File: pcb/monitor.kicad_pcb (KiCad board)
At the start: 2 copper layers, 111 parts, among them K1 DG128-02P, K101 DG128-02P, K102 DG128-02P, K103 DG128-02P, K104 DG128-02P, K105 DG128-02P, K106 DG128-02P, K107 DG128-02P, K108 DG128-02P, K109 DG128-02P, K110 DG128-02P, K111 DG128-02P, K112 DG128-02P, K113 JUMPER_3, K114 JUMPER_3, K2 DG128-02P, K3 DG128-02P, K4 DG128-02P, K5 DG128-02P, K6 DG128-02P, T1 ZUMT718, T10 ZUMT718, T101 ZUMT718, T102 ZUMT718, T2 ZUMT718, T3 ZUMT718, T4 ZUMT718, T5 ZUMT718, T6 ZUMT718, T7 ZUMT718, T8 ZUMT718, T9 ZUMT718, U1 LTC6803-3

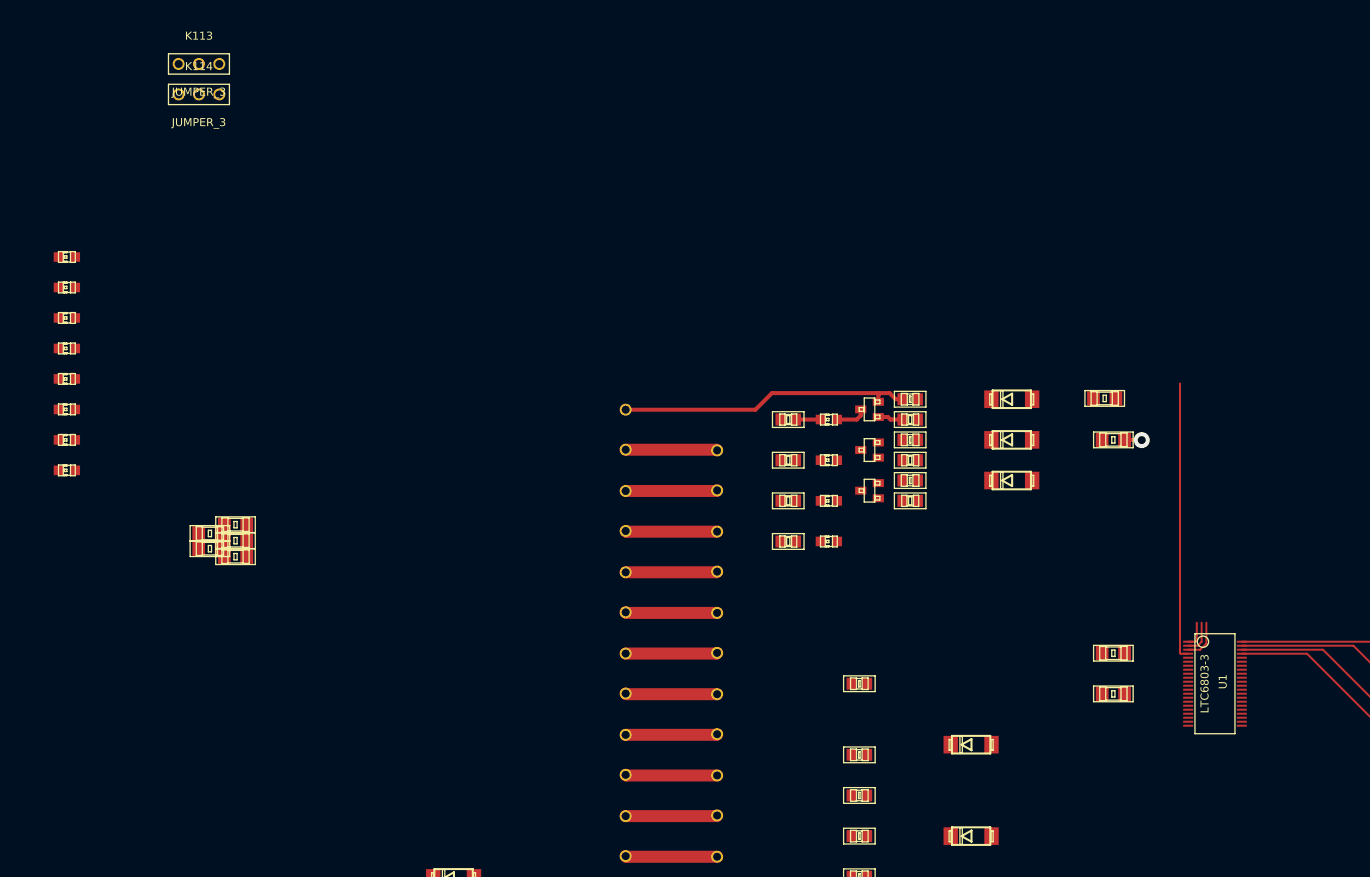
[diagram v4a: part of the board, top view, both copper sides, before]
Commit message: Change to 4 layer design
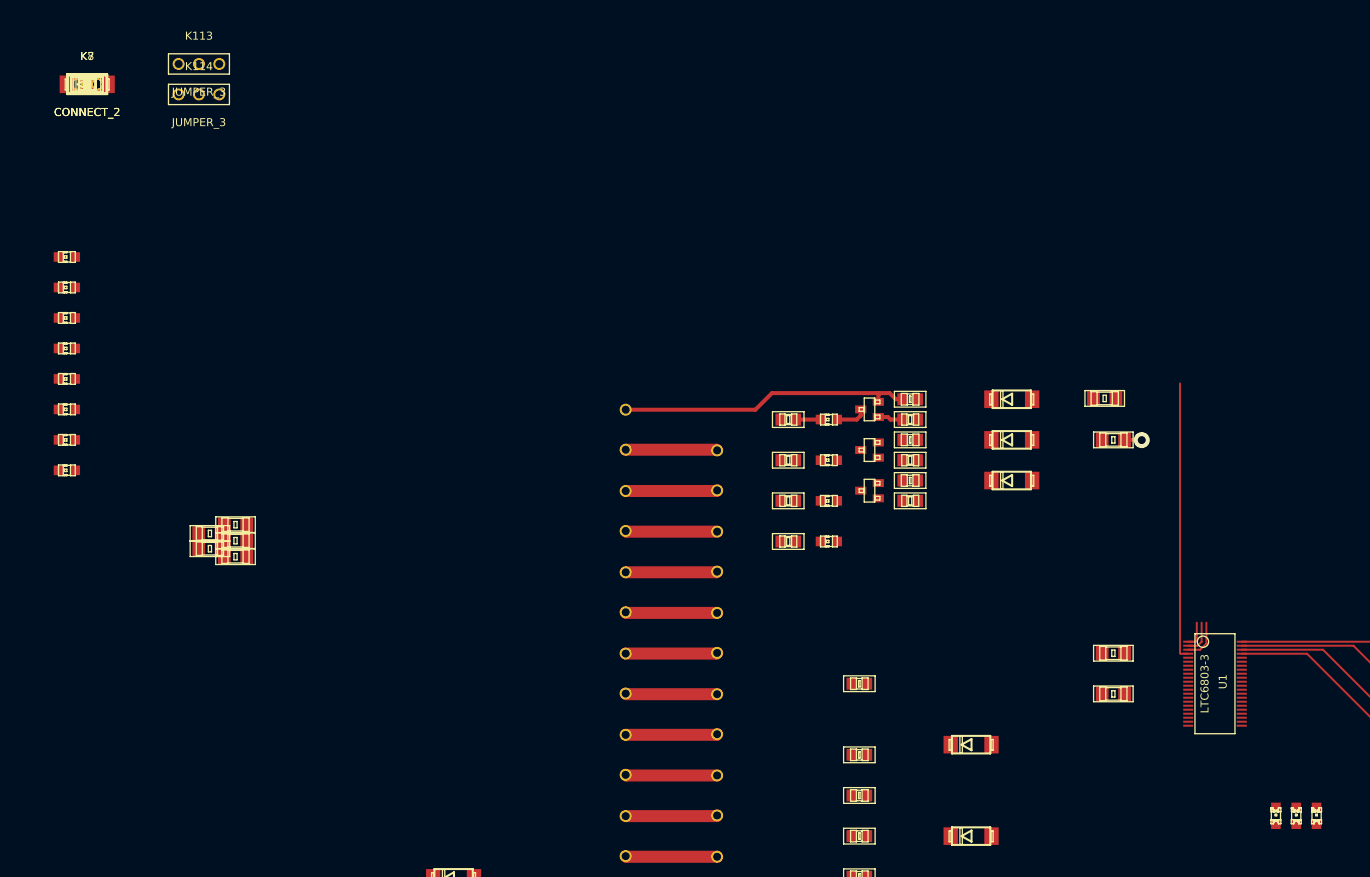
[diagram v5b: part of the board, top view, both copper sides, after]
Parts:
- added C1: 100n, oshec_rcl:rcl-C0805, F.Cu at (0.00, 0.00)
- added D4: CMHZ5265B, oshec_diode:diode-1-DO214AA, F.Cu at (0.00, 0.00)
- added K7, K8: CONNECT_2, Aalto_connect:CONNECT_2_2mm54_VERT, F.Cu at (0.00, 0.00)
- added L1: BLM31PG330SN1L, oshec_rcl:rcl-L1206, F.Cu at (0.00, 0.00)
- added LD13: LEDCHIPLED_0805, led-CHIPLED_0805, F.Cu at (153.7, 91.4)
- added LD14: LEDCHIPLED_0805, led-CHIPLED_0805, F.Cu at (151.1, 91.4)
- added LD15: LEDCHIPLED_0805, led-CHIPLED_0805, F.Cu at (148.6, 91.4)
- added R25, R26, R27: 220, oshec_rcl:rcl-R0805, F.Cu at (0.00, 0.00)
- added R28, R29: 200k, oshec_rcl:rcl-R0805, F.Cu at (0.00, 0.00)
- added R30, R31: 100, oshec_rcl:rcl-R0805, F.Cu at (0.00, 0.00)
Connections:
- K6 pad 2: /BATT1- -> GND
- R24 pad 2: /BATT1- -> GND
- T5 pad E: /BATT12+ -> /BATT6+
- U1 pad 30: GND -> /V-
- U1 pad 32: Net-(U1-Pad32) -> /Vtemp1
- U1 pad 33: Net-(U1-Pad33) -> /Vtemp2
- U1 pad 34: Net-(U1-Pad34) -> /Vref
- U1 pad 37: Net-(U1-Pad37) -> /WDTB
- U1 pad 38: Net-(U1-Pad38) -> /GPIO1
- U1 pad 39: Net-(U1-Pad39) -> /GPIO2
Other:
- copper layers 2 -> 4

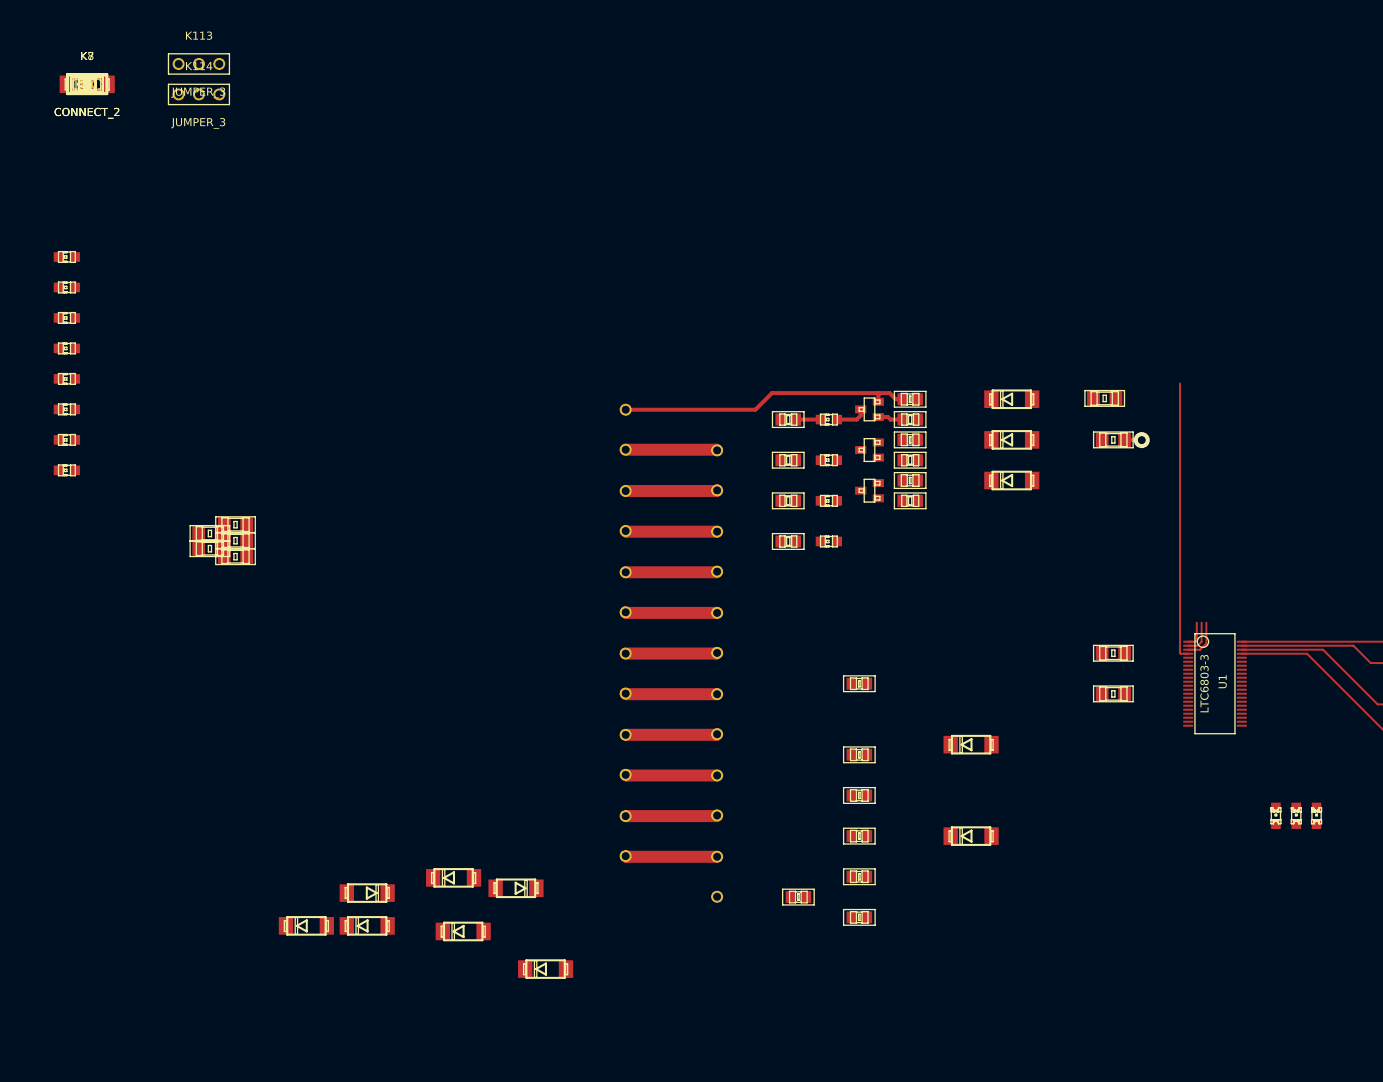
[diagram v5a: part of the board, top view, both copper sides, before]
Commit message: Add temperature + led connections
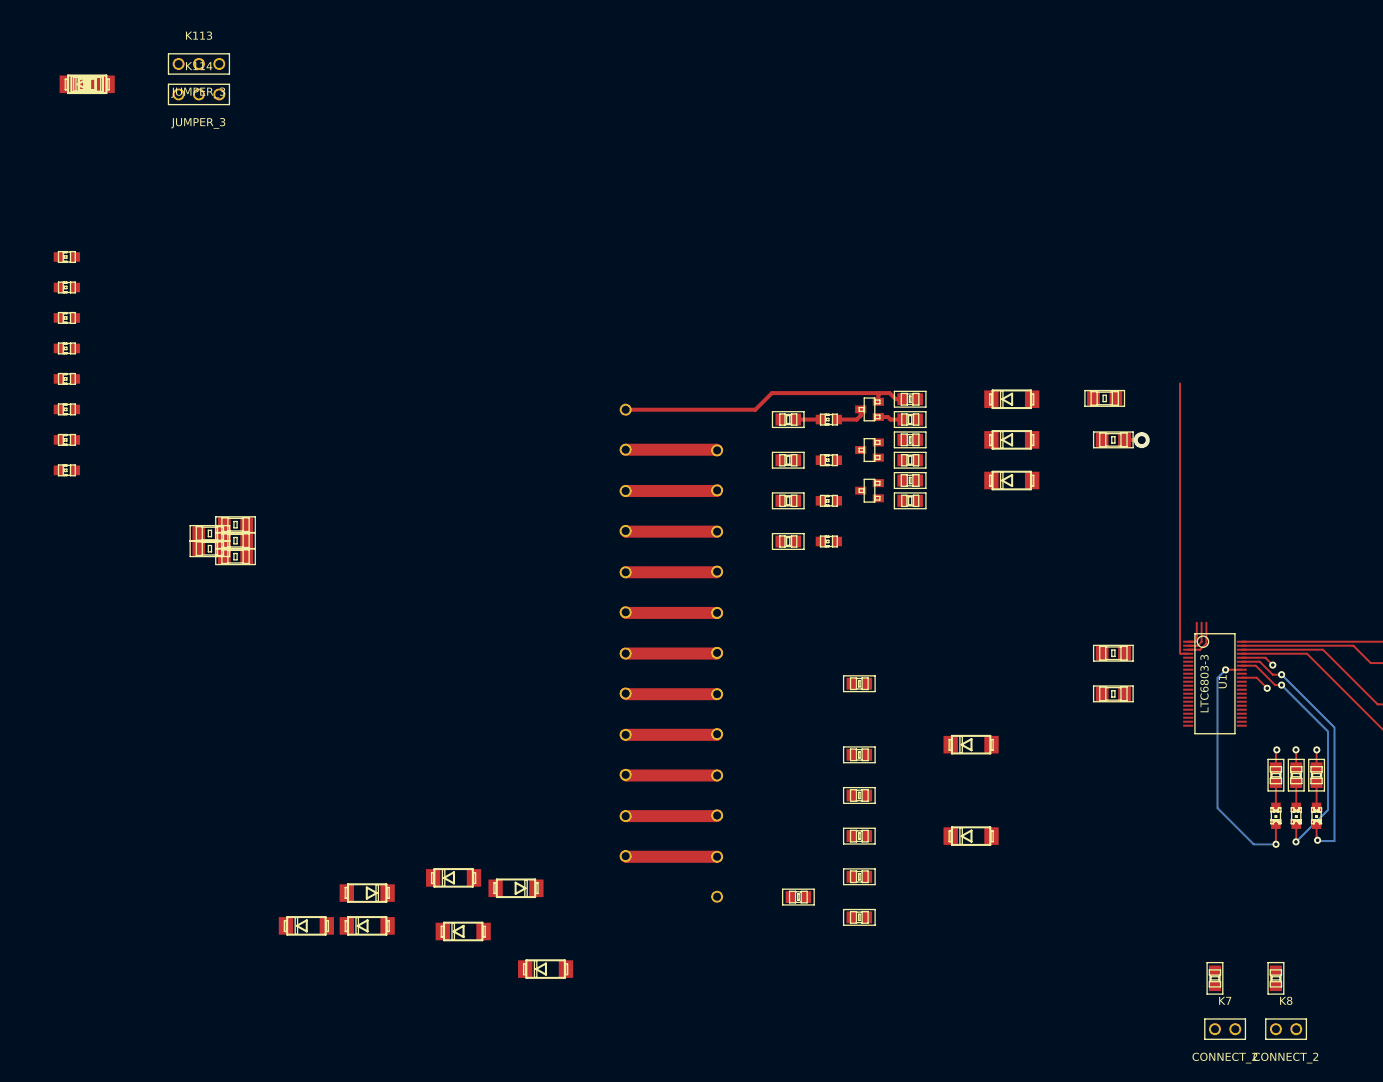
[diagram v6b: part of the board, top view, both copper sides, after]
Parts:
- moved K8 190.8 mm to (149.9, 118.1)
- moved R29 185.9 mm to (148.6, 111.8), turned to 90 degrees
- moved K7 184.9 mm to (142.2, 118.1)
- moved R28 179.9 mm to (141.0, 111.8), turned to 90 degrees
- moved R25 176.3 mm to (153.7, 86.4), turned to 270 degrees
- moved R26 174.1 mm to (151.1, 86.4), turned to 270 degrees
- moved R27 171.9 mm to (148.6, 86.4), turned to 270 degrees
- turned LD13 to 180 degrees
- turned LD14 to 180 degrees
- turned LD15 to 180 degrees
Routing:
- net /GPIO2: track 0.00 -> 33.4 mm, vias 0 -> 2
- net /GPIO1: track 0.00 -> 31.9 mm, vias 0 -> 2
- net /WDTB: track 0.00 -> 31.4 mm, vias 0 -> 2
- net /5V: track 0.00 -> 10.4 mm, vias 0 -> 4
- net /VMODE: track 0.00 -> 4.36 mm, vias 0 -> 1
- net Net-(LD15-PadA): track 0.00 -> 3.08 mm
- net Net-(LD14-PadA): track 0.00 -> 3.08 mm
- net Net-(LD13-PadA): track 0.00 -> 3.08 mm
- added copper zone on Inner1.Cu, net /5V

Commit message: Place grounds to PCB
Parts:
- removed C101, C102, C103, C104, C105, C106, C107, C108, C109, C110, C111, C112, C113: 3u3, oshec_rcl:rcl-C1206
- removed D101, D102, D103, D104, D105, D106, D107, D108, D109, D110, D111, D112: 7V5, oshec_diode:diode-1-DO214AA
- removed K1, K2: DG128-02P, Aalto_connect:CONNECT_2_5.00mm_SCREW_DG128-02P_DG128-5.0-02P-14-00A(H)
- removed LD1, LD10, LD11, LD12, LD2, LD3, LD4, LD5, LD6, LD7, LD8, LD9: GREEN-LED0805, oshec_led:led-CHIP-LED0805
- removed R1, R13, R14, R15, R16, R17, R18, R2, R3, R4, R5, R6: 10k, oshec_rcl:rcl-R0805
- removed R10, R11, R12, R19, R20, R21, R22, R23, R24, R7, R8, R9: 100, oshec_rcl:rcl-R0805
- removed R101, R102, R103, R104, R105, R106, R107, R108, R109, R110, R111, R112, R113: 10k, oshec_rcl:rcl-C0805
- removed R114: R-EU_R0805, oshec_rcl:rcl-C0805
- removed T1, T10, T101, T102, T2, T3, T4, T5, T6, T7, T8, T9: ZUMT718, oshec_transistor:transistor-SOT23-BEC
- added C301: 3u3, oshec_rcl:rcl-C1210, F.Cu at (111.8, 34.3)
- added C302: 3u3, oshec_rcl:rcl-C1210, F.Cu at (111.8, 44.5)
- added C303: 3u3, oshec_rcl:rcl-C1210, F.Cu at (111.8, 54.6)
- added C304, C305, C306, C310, C311: 3u3, oshec_rcl:rcl-C1210, F.Cu at (0.00, 0.00)
- added C307: 3u3, oshec_rcl:rcl-C1210, F.Cu at (111.8, 95.2)
- added C308: 3u3, oshec_rcl:rcl-C1210, F.Cu at (111.8, 105.4)
- added C309: 3u3, oshec_rcl:rcl-C1210, F.Cu at (121.9, 97.8)
- added C312: 3u3, oshec_rcl:rcl-C1210, F.Cu at (152.4, 96.5)
- added C313: 3u3, oshec_rcl:rcl-C1210, F.Cu at (166.4, 116.8)
- added C401: 10u, oshec_rcl:rcl-C0805, F.Cu at (170.2, 80.0)
- added C402: 100n, oshec_rcl:rcl-C0402, F.Cu at (167.8, 78.7)
- added C403: 10u, oshec_rcl:rcl-C0805, F.Cu at (152.4, 78.7)
- added C404: 100n, oshec_rcl:rcl-C0402, F.Cu at (154.8, 78.7)
- added D301: 7V5, oshec_diode:diode-1-DO214AA, F.Cu at (106.7, 36.8)
- added D302: 7V5, oshec_diode:diode-1-DO214AA, F.Cu at (106.7, 47.0)
- added D303: 7V5, oshec_diode:diode-1-DO214AA, F.Cu at (106.7, 57.1)
- added D304, D305, D306, D310, D311: 7V5, oshec_diode:diode-1-DO214AA, F.Cu at (0.00, 0.00)
- added D307: 7V5, oshec_diode:diode-1-DO214AA, F.Cu at (106.7, 97.8)
- added D308: 7V5, oshec_diode:diode-1-DO214AA, F.Cu at (107.0, 108.0)
- added D309: 7V5, oshec_diode:diode-1-DO214AA, F.Cu at (124.5, 102.9)
- added D312: 7V5, oshec_diode:diode-1-DO214AA, F.Cu at (154.9, 101.6)
- added D313: 7V5, oshec_diode:diode-1-DO214AA, F.Cu at (170.2, 116.8)
- added D401: 1N4004, oshec_diode:diode-1-DO214AA, F.Cu at (0.00, 0.00)
- added K401: DG128-02P, Aalto_connect:CONNECT_2_5.00mm_SCREW_DG128-02P_DG128-5.0-02P-14-00A(H), F.Cu at (179.1, 85.1)
- added K402: DG128-02P, Aalto_connect:CONNECT_2_5.00mm_SCREW_DG128-02P_DG128-5.0-02P-14-00A(H), F.Cu at (179.1, 74.9)
- added K403: DG128-02P, Aalto_connect:CONNECT_2_5.00mm_SCREW_DG128-02P_DG128-5.0-02P-14-00A(H), F.Cu at (179.1, 64.8)
- added LD201: GREEN-LED0805, oshec_led:led-CHIPLED_0805, F.Cu at (102.9, 39.4)
- added LD202: GREEN-LED0805, oshec_led:led-CHIPLED_0805, F.Cu at (102.9, 100.3)
- added LD203: GREEN-LED0805, oshec_led:led-CHIPLED_0805, F.Cu at (102.9, 49.5)
- added LD204: GREEN-LED0805, oshec_led:led-CHIPLED_0805, F.Cu at (102.9, 110.5)
- added LD205: GREEN-LED0805, oshec_led:led-CHIPLED_0805, F.Cu at (127.0, 106.7)
- added LD206, LD207, LD208, LD209, LD210, LD211: GREEN-LED0805, oshec_led:led-CHIPLED_0805, F.Cu at (0.00, 0.00)
- added LD212: GREEN-LED0805, oshec_led:led-CHIPLED_0805, F.Cu at (157.5, 106.7)
- added R201: 10k, oshec_rcl:rcl-C0805, F.Cu at (111.8, 39.4)
- added R202: 10k, oshec_rcl:rcl-C0805, F.Cu at (111.8, 100.3)
- added R203: 100, oshec_rcl:rcl-C0805, F.Cu at (97.8, 39.4)
- added R204: 100, oshec_rcl:rcl-C0805, F.Cu at (97.8, 100.3)
- added R205: 10k, oshec_rcl:rcl-C0805, F.Cu at (111.8, 49.5)
- added R206: 10k, oshec_rcl:rcl-C0805, F.Cu at (111.8, 110.5)
- added R207: 100, oshec_rcl:rcl-C0805, F.Cu at (97.8, 49.5)
- added R208: 100, oshec_rcl:rcl-C0805, F.Cu at (97.8, 110.5)
- added R209: 10k, oshec_rcl:rcl-C0805, F.Cu at (127.0, 97.8)
- added R210: 10k, oshec_rcl:rcl-C0805, F.Cu at (111.8, 59.7)
- added R211: 100, oshec_rcl:rcl-C0805, F.Cu at (127.0, 111.8)
- added R212: 100, oshec_rcl:rcl-C0805, F.Cu at (97.8, 59.7)
- added R213, R214, R217, R218, R221: 10k, oshec_rcl:rcl-C0805, F.Cu at (0.00, 0.00)
- added R215, R216, R219, R220, R223: 100, oshec_rcl:rcl-C0805, F.Cu at (0.00, 0.00)
- added R222: 10k, oshec_rcl:rcl-C0805, F.Cu at (157.5, 96.5)
- added R224: 100, oshec_rcl:rcl-C0805, F.Cu at (157.5, 111.8)
- added R301: 10k, oshec_rcl:rcl-C0805, F.Cu at (97.8, 34.3)
- added R302: 10k, oshec_rcl:rcl-C0805, F.Cu at (97.8, 44.5)
- added R303: 10k, oshec_rcl:rcl-C0805, F.Cu at (97.8, 54.6)
- added R304: 10k, oshec_rcl:rcl-C0805, F.Cu at (97.8, 64.8)
- added R305: 10k, oshec_rcl:rcl-C0805, F.Cu at (97.8, 74.9)
- added R306: 10k, oshec_rcl:rcl-C0805, F.Cu at (97.8, 85.1)
- added R307: 10k, oshec_rcl:rcl-C0805, F.Cu at (97.8, 95.2)
- added R308: 10k, oshec_rcl:rcl-C0805, F.Cu at (97.8, 105.4)
- added R309: 10k, oshec_rcl:rcl-C0805, F.Cu at (121.9, 111.8)
- added R310: 10k, oshec_rcl:rcl-C0805, F.Cu at (132.1, 111.8)
- added R311: 10k, oshec_rcl:rcl-C0805, F.Cu at (142.2, 111.8)
- added R312: 10k, oshec_rcl:rcl-C0805, F.Cu at (152.4, 111.8)
- added R313: 10k, oshec_rcl:rcl-C1210, F.Cu at (162.6, 116.8)
- added T201: ZUMT718, oshec_transistor:transistor-SOT23-BEC, F.Cu at (102.9, 35.6)
- added T202: ZUMT718, oshec_transistor:transistor-SOT23-BEC, F.Cu at (102.9, 96.5)
- added T203: ZUMT718, oshec_transistor:transistor-SOT23-BEC, F.Cu at (102.9, 45.7)
- added T204: ZUMT718, oshec_transistor:transistor-SOT23-BEC, F.Cu at (102.9, 106.7)
- added T205: ZUMT718, oshec_transistor:transistor-SOT23-BEC, F.Cu at (123.2, 106.7)
- added T206, T207, T208, T209, T210, T211: ZUMT718, oshec_transistor:transistor-SOT23-BEC, F.Cu at (0.00, 0.00)
- added T212: ZUMT718, oshec_transistor:transistor-SOT23-BEC, F.Cu at (153.7, 106.7)
- added TP101: TEST_POINT, Aalto_connect:Keystone_Electronics_5000, F.Cu at (149.0, 80.0)
- added TP102: TEST_POINT, Aalto_connect:Keystone_Electronics_5000, F.Cu at (144.0, 67.0)
- added TP103: TEST_POINT, Aalto_connect:Keystone_Electronics_5000, F.Cu at (144.0, 73.0)
- added TP104: TEST_POINT, Aalto_connect:Keystone_Electronics_5000, F.Cu at (144.0, 83.0)
- added TP105: TEST_POINT, Aalto_connect:Keystone_Electronics_5000, F.Cu at (144.0, 76.0)
- added TP106: TEST_POINT, Aalto_connect:Keystone_Electronics_5000, F.Cu at (150.0, 70.0)
- added TP107, TP108, TP109, TP110, TP111, TP112, TP113: TEST_POINT, Aalto_connect:Keystone_Electronics_5000, F.Cu at (135.0, 135.1)
- added U401: ADUM5401, Aalto_ic:SOIC_16_WIDE, F.Cu at (161.3, 74.9)
- K101, K102, K103, K104, K105, K106, K107, K108, K109, K110, K111, K112, K3, K4, K5, K6: moved to F.Cu
- K7, K8: footprint Aalto_connect:CONNECT_2_2mm54_VERT -> Aalto_connect:CONNECT_2_5.00mm_SCREW_DG128-02P_DG128-5.0-02P-14-00A(H)
- LD13, LD14, LD15: footprint led-CHIPLED_0805 -> oshec_led:led-CHIP-LED0805
- R30, R31: footprint oshec_rcl:rcl-R0805 -> oshec_rcl:rcl-R1210
- moved C1 157.9 mm to (134.6, 82.5), turned to 180 degrees
- moved R31 150.3 mm to (141.0, 52.1), turned to 90 degrees
- moved L1 148.2 mm to (141.0, 45.7), turned to 270 degrees
- moved R30 145.8 mm to (134.6, 55.9), turned to 180 degrees
- moved D4 143.9 mm to (134.6, 50.8), turned to 180 degrees
- moved D1 98.4 mm to (135.0, 135.1)
- moved D2 93.6 mm to (135.0, 135.1)
- moved D3 89.0 mm to (135.0, 135.1)
- moved K111 81.5 mm to (144.8, 119.4), turned to 180 degrees
- moved K112 78.9 mm to (154.9, 119.4), turned to 180 degrees
- moved K109 67.3 mm to (124.5, 119.4), turned to 180 degrees
- moved K110 63.7 mm to (134.6, 119.4), turned to 180 degrees
- moved R25 52.1 mm to (135.0, 135.1), turned to 0 degrees
- moved R26 51.3 mm to (135.0, 135.1), turned to 0 degrees
- moved R27 50.6 mm to (135.0, 135.1), turned to 0 degrees
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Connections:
- net /5V renamed /Isolation/5V
- net /BATT1+ renamed /Lowpass/BATT1+
- net /BATT10+ renamed /Lowpass/BATT10+
- net /BATT11+ renamed /Lowpass/BATT11+
- net /BATT12+ renamed /discharge/BATT12+
- net /BATT2+ renamed /Lowpass/BATT2+
- net /BATT3+ renamed /Lowpass/BATT3+
- net /BATT4+ renamed /Lowpass/BATT4+
- net /BATT5+ renamed /Lowpass/BATT5+
- net /BATT6+ renamed /Lowpass/BATT6+
- net /BATT7+ renamed /Lowpass/BATT7+
- net /BATT8+ renamed /Lowpass/BATT8+
- net /BATT9+ renamed /Lowpass/BATT9+
- net /CSBI renamed /Isolation/CSBI
- net /SCKI renamed /Isolation/SCKI
- net /SDI renamed /Isolation/SDI
- C1 pad 1: /V- -> DGND
- D4 pad A: GND -> AGND
- K112 pad 2: GND -> AGND
- K6 pad 2: GND -> DGND
- K7 pad 2: GND -> AGND
- K8 pad 2: GND -> AGND
- R30 pad 1: /V- -> DGND
- R30 pad 2: GND -> AGND
- U1 pad 10: /S10 -> /discharge/S10
- U1 pad 11: Net-(C104-Pad2) -> /Lowpass/C9
- U1 pad 12: /S9 -> /discharge/S9
- U1 pad 13: Net-(C105-Pad2) -> /Lowpass/C8
- U1 pad 14: /S8 -> /discharge/S8
- U1 pad 15: Net-(C106-Pad2) -> /Lowpass/C7
- U1 pad 16: /S7 -> /discharge/S7
- U1 pad 17: Net-(C107-Pad2) -> /Lowpass/C6
- U1 pad 18: /S6 -> /discharge/S6
- U1 pad 19: Net-(C108-Pad2) -> /Lowpass/C5
- U1 pad 20: /S5 -> /discharge/S5
- U1 pad 21: Net-(C109-Pad2) -> /Lowpass/C4
- U1 pad 22: /S4 -> /discharge/S4
- U1 pad 23: Net-(C110-Pad2) -> /Lowpass/C3
- U1 pad 24: /S3 -> /discharge/S3
- U1 pad 25: Net-(C111-Pad2) -> /Lowpass/C2
- U1 pad 26: /S2 -> /discharge/S2
- U1 pad 27: Net-(C112-Pad2) -> /Lowpass/C1
- U1 pad 28: /S1 -> /discharge/S1
- U1 pad 29: Net-(C113-Pad2) -> /Lowpass/C0
- U1 pad 30: /V- -> DGND
- U1 pad 43: /SDO -> /Isolation/SDO
- U1 pad 5: Net-(C101-Pad2) -> /Lowpass/C12
- U1 pad 6: /S12 -> /discharge/S12
- U1 pad 7: Net-(C102-Pad2) -> /Lowpass/C11
- U1 pad 8: /S11 -> /discharge/S11
- U1 pad 9: Net-(C103-Pad2) -> /Lowpass/C10
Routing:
- net /Lowpass/C11: track 0.00 -> 74.6 mm
- net /Lowpass/C12: track 0.00 -> 70.9 mm
- net /Lowpass/C10: track 0.00 -> 50.8 mm
- net /discharge/S12: track 0.00 -> 50.7 mm
- net /discharge/S5: track 0.00 -> 41.7 mm
- net /discharge/S11: track 0.00 -> 40.4 mm
- net /Lowpass/C5: track 0.00 -> 38.6 mm
- net /SDO: track 36.9 -> 0.00 mm
- net /GPIO2: track 33.4 -> 0.00 mm, vias 2 -> 0
- net /discharge/S6: track 0.00 -> 32.5 mm
- net /GPIO1: track 31.9 -> 0.00 mm, vias 2 -> 0
- net /WDTB: track 31.4 -> 0.00 mm, vias 2 -> 0
- net AGND: track 0.00 -> 30.6 mm, vias 0 -> 4
- net /discharge/S10: track 0.00 -> 30.4 mm
- net /Lowpass/C6: track 0.00 -> 30.4 mm
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- added copper zone on Inner2.Cu, net /Isolation/GND1
- added copper zone on Inner2.Cu, net AGND
- added copper zone on Inner2.Cu, net DGND
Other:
- board outline added: 100 x 100 mm
- net class AGND added: clearance 1, trace_width 0.2032, via_dia 0.889, via_drill 0.635
- net class Default: clearance 0.245 -> 0.2032; trace_width 0.245 -> 0.2032
- rule trace_clearance: 0.245 -> 0.2032
- rule trace_min: 0.245 -> 0.2032
- rule via_min_drill: 0.508 -> 0.3
- rule via_min_size: 0.889 -> 0.5
- board text added: "Isolation boundary - do not cross"
- board text removed: "ISOLATE ?"
- board text removed: "No tracks allowed inside rectangles except ground"

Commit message: Remove groundplanes
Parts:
- moved TP107 57.5 mm to (149.2, 79.4)
- moved C1 15.2 mm to (134.6, 67.3)
- moved TP104 11.9 mm to (152.4, 91.4)
- moved TP106 10.3 mm to (142.2, 76.8)
- moved TP102 9.83 mm to (151.8, 73.0)
- moved TP105 4.90 mm to (148.6, 74.3)
- moved TP101 3.02 mm to (146.1, 80.6)
- moved TP103 2.93 mm to (145.4, 75.6)
- moved K7 2.75 mm to (155.0, 135.0)
- moved C403 1.27 mm to (152.4, 80.0)
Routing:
- net /Isolation/SCKI: track 56.9 -> 21.2 mm
- net /Isolation/SDI: track 55.7 -> 20.9 mm
- net /Isolation/CSBI: track 56.3 -> 27.1 mm, vias 2 -> 1
- net AGND: track 30.6 -> 41.5 mm, vias 4 -> 7
- net /Isolation/5V: track 7.36 -> 16.3 mm, vias 1 -> 2
- net /V+: track 13.4 -> 5.60 mm
- net /Lowpass/BATT4+: track 5.47 -> 0.00 mm
- net DGND: track 14.3 -> 9.67 mm
- removed copper zone on Inner2.Cu, net /Isolation/GND1
- removed copper zone on Inner2.Cu, net AGND
- removed copper zone on Inner2.Cu, net DGND
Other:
- board text added: "Do not cross"
- board text added: "Isolation boundary"
- board text removed: "Isolation boundary - do not cross"
- board text removed: "Through-hole components are flipped They're on bottom side of board. This way they get soldered to front"
